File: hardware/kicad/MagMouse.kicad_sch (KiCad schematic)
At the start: 0 parts

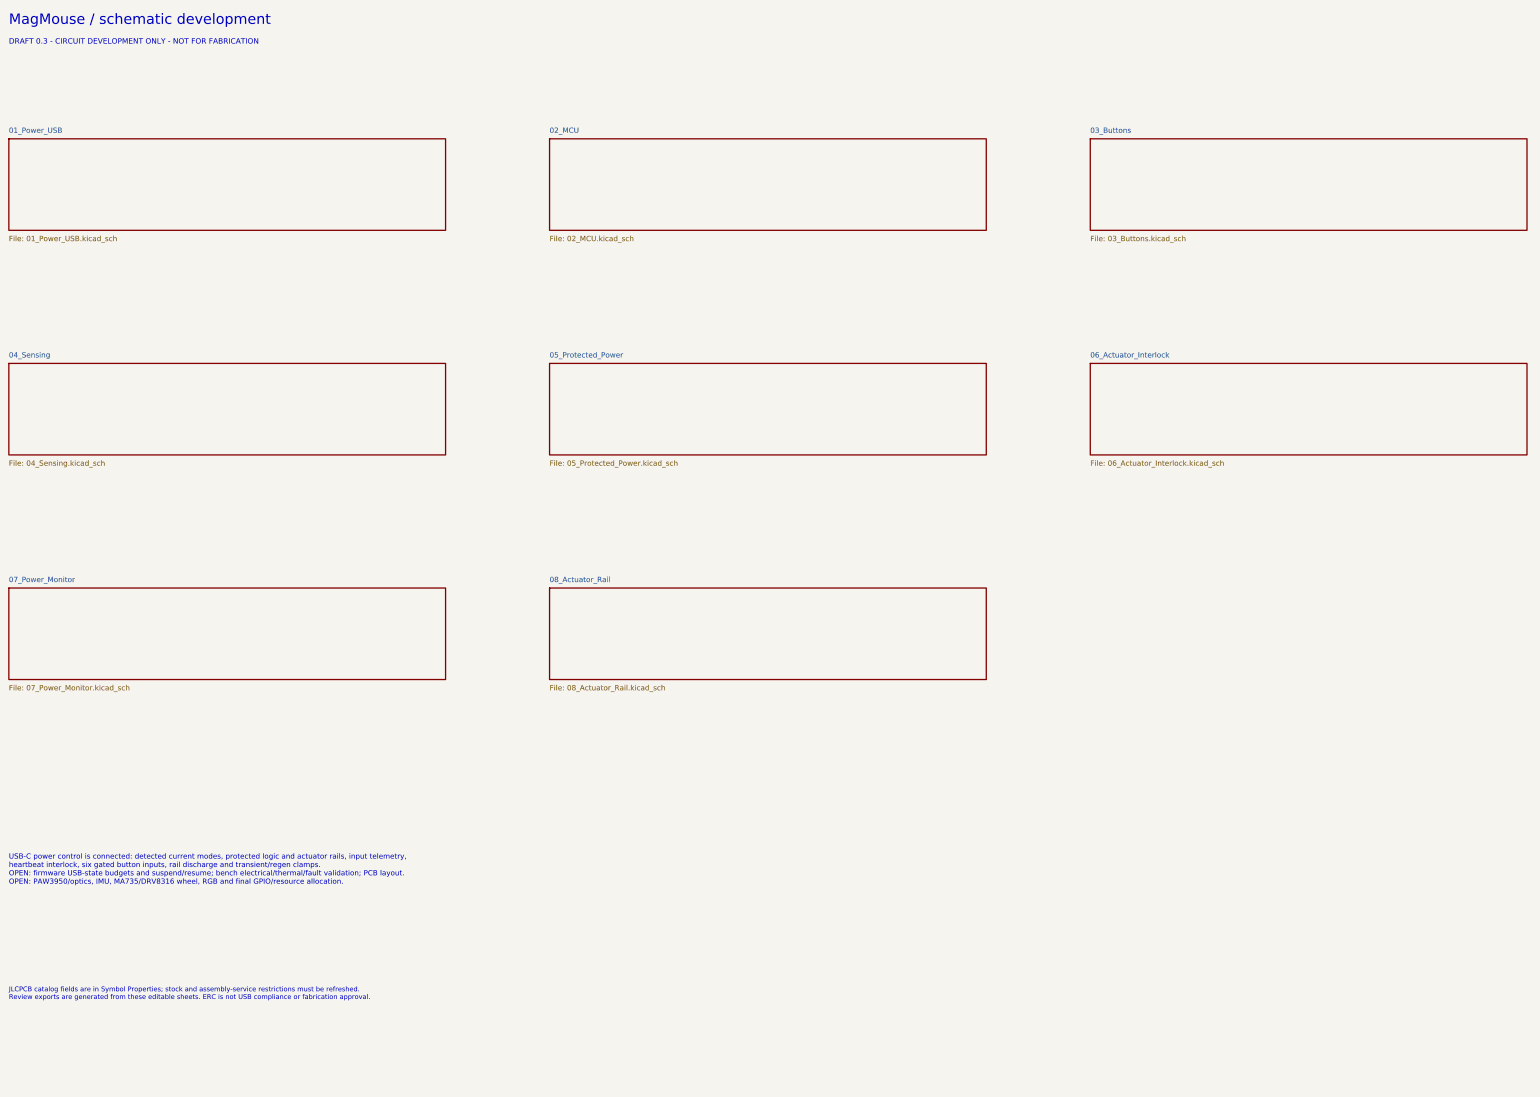
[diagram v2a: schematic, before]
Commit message: Allocate ESP32-S3 GPIO and peripheral resources
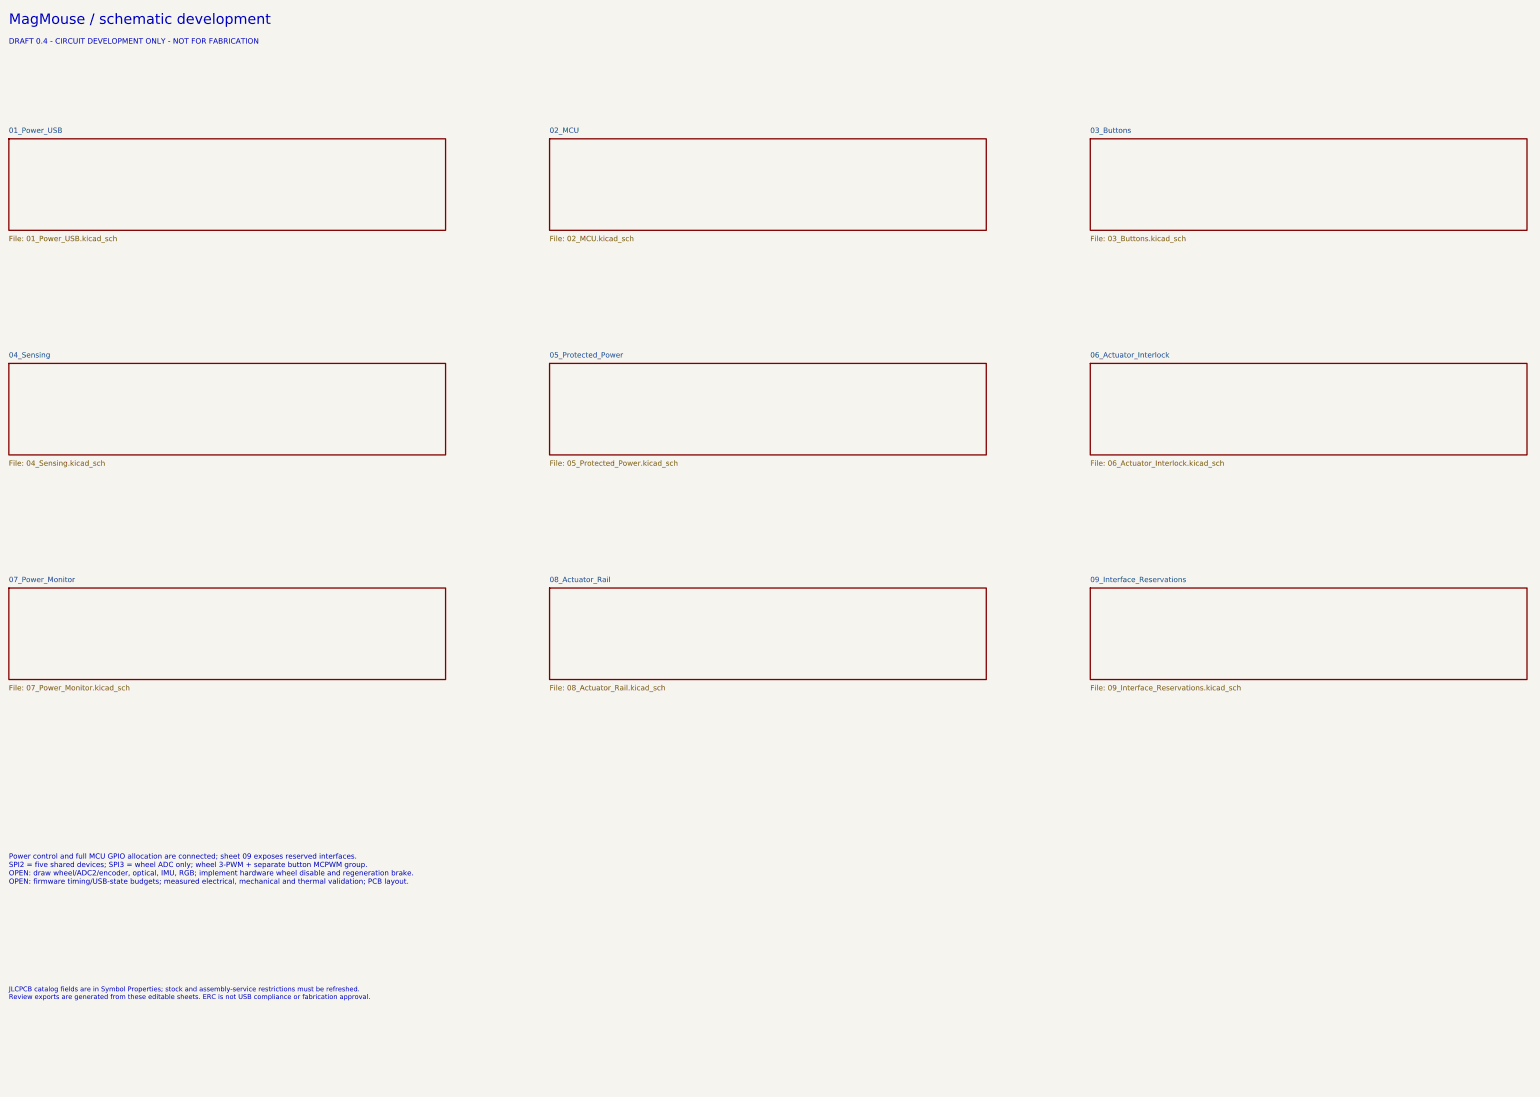
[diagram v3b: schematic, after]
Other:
- added sheet 09_Interface_Reservations (09_Interface_Reservations.kicad_sch)
- note added: "DRAFT 0.4 - CIRCUIT DEVELOPMENT ONLY - NOT FOR FABRICATION"
- note added: "Power control and full MCU GPIO allocation are connected; sheet 09 exposes reserved interfaces. SPI2 = five shared devices; SPI3 = wheel ADC only; wheel 3-PWM + separate button MCPWM group. OPEN: draw wheel/ADC2/encoder, optical, IMU, RGB; implement hardware wheel disable and regeneration brake. OPEN: firmware timing/USB-state budgets; measured electrical, mechanical and thermal validation; PCB l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"
- note removed: "DRAFT 0.3 - CIRCUIT DEVELOPMENT ONLY - NOT FOR FABRICATION"
- note removed: "USB-C power control is connected: detected current modes, protected logic and actuator rails, input telemetry, heartbeat interlock, six gated button inputs, rail discharge and transient/regen clamps. OPEN: firmware USB-state budgets and suspend/resume; bench electrical/thermal/fault validation; PCB layout. OPEN: PAW3950/optics, IMU, MA735/DRV8316 wheel, RGB and final GPIO/resource allocation."
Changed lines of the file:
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@@
     (title "MagMouse - MagMouse")
     (date "2026-09-08")
-    (rev "0.3 DRAFT")
+    (rev "0.4 DRAFT")
     (company "MagMouse")
     (comment 1 "NOT FOR FABRICATION - unresolved circuits listed in README.md"))
@@
       (justify left top))
 )
-  (text "DRAFT 0.3 - CIRCUIT DEVELOPMENT ONLY - NOT FOR FABRICATION"
+  (text "DRAFT 0.4 - CIRCUIT DEVELOPMENT ONLY - NOT FOR FABRICATION"
     (at 20 24 0)
     (effects
@@
         (path "/5d73110b-42e6-5c5c-9841-c82d60f67640"
           (page "9")))))
-  (text "USB-C power control is connected: detected current modes, protected logic and actuator rails, input telemetry,\nheartbeat interlock, six gated button inputs, rail discharge and transient/regen clamps.\nOPEN: firmware USB-state budgets and suspend/resume; bench electrical/thermal/fault validation; PCB layout.\nOPEN: PAW3950/optics, IMU, MA735/DRV8316 wheel, RGB and final GPIO/resource allocation."
+  (text "Power control and full MCU GPIO allocation are connected; sheet 09 exposes reserved interfaces.\nSPI2 = five shared devices; SPI3 = wheel ADC only; wheel 3-PWM + separate button MCPWM group.\nOPEN: draw wheel/ADC2/encoder, optical, IMU, RGB; implement hardware wheel disable and regeneration brake.\nOPEN: firmware timing/USB-state budgets; measured electrical, mechanical and thermal validation; PCB layout."
     (at 20 220 0)
     (effects
@@
     (path "/"
       (page "1")))
-  (embedded_fonts no))
+  (embedded_fonts no)
+  (sheet
+    (at 280 156)
+    (size 105 22)
+    (stroke
+      (width 0.254)
+      (type default))
+    (fill
+      (color 0 0 0 0))
+    (property "Sheetname" "09_Interface_Reservations"
+      (at 280 154.73 0)
+      (effects
+        (font
+          (size 1.27 1.27))
+        (justify left bottom)))
+    (property "Sheetfile" "09_Interface_Reservations.kicad_sch"
+      (at 280 179.27 0)
+      (effects
+        (font
+          (size 1.27 1.27))
+        (justify left top)))
+    (instances
+      (project "MagMouse"
+        (path "/5d73110b-42e6-5c5c-9841-c82d60f67640"
+          (page "10"))))))

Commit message: Add wheel control circuitry and autonomous regeneration brake
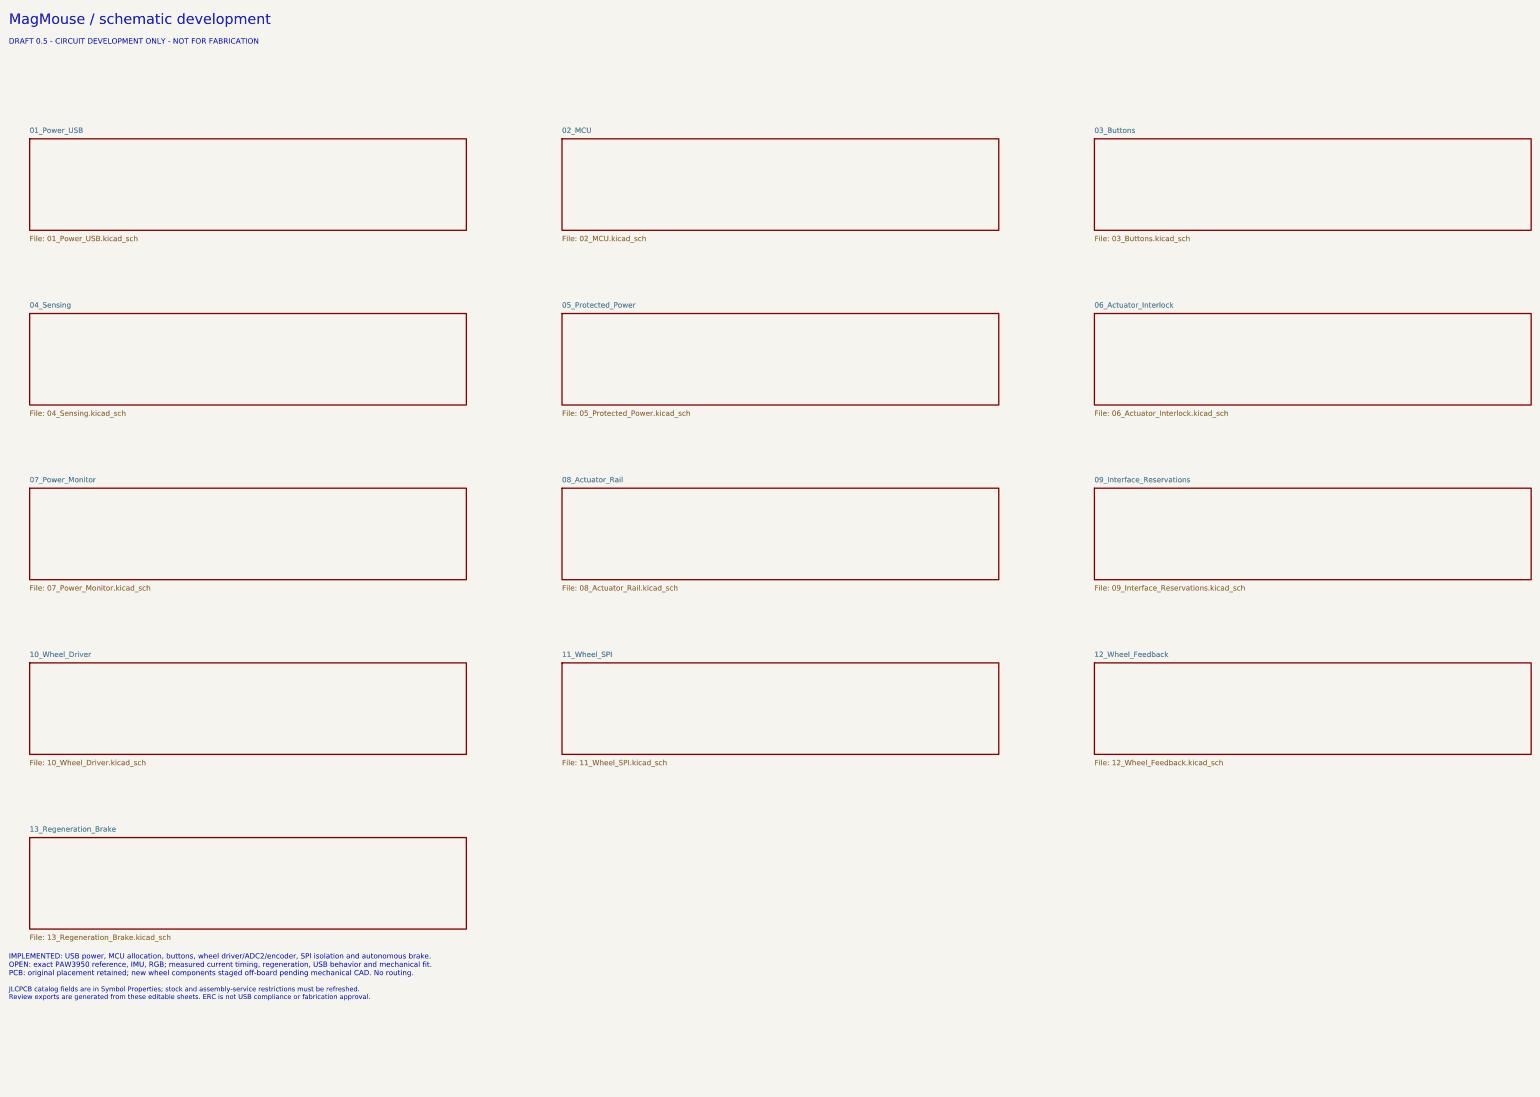
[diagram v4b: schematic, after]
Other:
- added sheet 10_Wheel_Driver (10_Wheel_Driver.kicad_sch)
- added sheet 11_Wheel_SPI (11_Wheel_SPI.kicad_sch)
- added sheet 12_Wheel_Feedback (12_Wheel_Feedback.kicad_sch)
- added sheet 13_Regeneration_Brake (13_Regeneration_Brake.kicad_sch)
- note added: "DRAFT 0.5 - CIRCUIT DEVELOPMENT ONLY - NOT FOR FABRICATION"
- note added: "IMPLEMENTED: USB power, MCU allocation, buttons, wheel driver/ADC2/encoder, SPI isolation and autonomous brake. OPEN: exact PAW3950 reference, IMU, RGB; measured current timing, regeneration, USB behavior and mechanical fit. PCB: original placement retained; new wheel components staged off-board pending mechanical CAD. No routing."
- note removed: "DRAFT 0.4 - CIRCUIT DEVELOPMENT ONLY - NOT FOR FABRICATION"
- note removed: "Power control and full MCU GPIO allocation are connected; sheet 09 exposes reserved interfaces. SPI2 = five shared devices; SPI3 = wheel ADC only; wheel 3-PWM + separate button MCPWM group. OPEN: draw wheel/ADC2/encoder, optical, IMU, RGB; implement hardware wheel disable and regeneration brake. OPEN: firmware timing/USB-state budgets; measured electrical, mechanical and thermal validation; PCB l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"
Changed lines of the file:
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@@
   (title_block
     (title "MagMouse - MagMouse")
-    (date "2026-09-08")
-    (rev "0.4 DRAFT")
+    (date "2026-09-09")
+    (rev "0.5 DRAFT")
     (company "MagMouse")
     (comment 1 "NOT FOR FABRICATION - unresolved circuits listed in README.md"))
@@
       (justify left top))
 )
-  (text "DRAFT 0.4 - CIRCUIT DEVELOPMENT ONLY - NOT FOR FABRICATION"
+  (text "DRAFT 0.5 - CIRCUIT DEVELOPMENT ONLY - NOT FOR FABRICATION"
     (at 20 24 0)
     (effects
@@
 )
   (sheet
-    (at 20 48)
+    (at 25 48)
     (size 105 22)
     (stroke
@@
       (color 0 0 0 0))
     (property "Sheetname" "01_Power_USB"
-      (at 20 46.73 0)
+      (at 25 46.73 0)
       (effects
         (font
@@
         (justify left bottom)))
     (property "Sheetfile" "01_Power_USB.kicad_sch"
-      (at 20 71.27 0)
+      (at 25 71.27 0)
       (effects
         (font
@@
           (page "2")))))
   (sheet
-    (at 150 48)
+    (at 153 48)
     (size 105 22)
     (stroke
@@
       (color 0 0 0 0))
     (property "Sheetname" "02_MCU"
-      (at 150 46.73 0)
+      (at 153 46.73 0)
       (effects
         (font
@@
         (justify left bottom)))
     (property "Sheetfile" "02_MCU.kicad_sch"
-      (at 150 71.27 0)
+      (at 153 71.27 0)
       (effects
         (font
@@
           (page "3")))))
   (sheet
-    (at 280 48)
+    (at 281 48)
     (size 105 22)
     (stroke
@@
       (color 0 0 0 0))
     (property "Sheetname" "03_Buttons"
-      (at 280 46.73 0)
+      (at 281 46.73 0)
       (effects
         (font
@@
         (justify left bottom)))
     (property "Sheetfile" "03_Buttons.kicad_sch"
-      (at 280 71.27 0)
+      (at 281 71.27 0)
       (effects
         (font
@@
           (page "4")))))
   (sheet
-    (at 20 102)
+    (at 25 90)
     (size 105 22)
     (stroke
@@
       (color 0 0 0 0))
     (property "Sheetname" "04_Sensing"
-      (at 20 100.73 0)
+      (at 25 88.73 0)
       (effects
         (font
@@
         (justify left bottom)))
     (property "Sheetfile" "04_Sensing.kicad_sch"
-      (at 20 125.27 0)
+      (at 25 113.27 0)
       (effects
         (font
@@
           (page "5")))))
   (sheet
-    (at 150 102)
+    (at 153 90)
     (size 105 22)
     (stroke
@@
       (color 0 0 0 0))
     (property "Sheetname" "05_Protected_Power"
-      (at 150 100.73 0)
+      (at 153 88.73 0)
       (effects
         (font
@@
         (justify left bottom)))
     (property "Sheetfile" "05_Protected_Power.kicad_sch"
-      (at 150 125.27 0)
+      (at 153 113.27 0)
       (effects
         (font
@@
           (page "6")))))
   (sheet
-    (at 280 102)
+    (at 281 90)
     (size 105 22)
     (stroke
@@
       (color 0 0 0 0))
     (property "Sheetname" "06_Actuator_Interlock"
-      (at 280 100.73 0)
+      (at 281 88.73 0)
       (effects
         (font
@@
         (justify left bottom)))
     (property "Sheetfile" "06_Actuator_Interlock.kicad_sch"
-      (at 280 125.27 0)
+      (at 281 113.27 0)
       (effects
         (font
@@
           (page "7")))))
   (sheet
-    (at 20 156)
+    (at 25 132)
     (size 105 22)
     (stroke
@@
       (color 0 0 0 0))
     (property "Sheetname" "07_Power_Monitor"
-      (at 20 154.73 0)
+      (at 25 130.73 0)
       (effects
         (font
@@
         (justify left bottom)))
     (property "Sheetfile" "07_Power_Monitor.kicad_sch"
-      (at 20 179.27 0)
+      (at 25 155.27 0)
       (effects
         (font
@@
           (page "8")))))
   (sheet
-    (at 150 156)
+    (at 153 132)
     (size 105 22)
     (stroke
@@
       (color 0 0 0 0))
     (property "Sheetname" "08_Actuator_Rail"
-      (at 150 154.73 0)
+      (at 153 130.73 0)
       (effects
         (font
@@
         (justify left bottom)))
     (property "Sheetfile" "08_Actuator_Rail.kicad_sch"
-      (at 150 179.27 0)
+      (at 153 155.27 0)
       (effects
         (font
@@
         (path "/5d73110b-42e6-5c5c-9841-c82d60f67640"
           (page "9")))))
-  (text "Power control and full MCU GPIO allocation are connected; sheet 09 exposes reserved interfaces.\nSPI2 = five shared devices; SPI3 = wheel ADC only; wheel 3-PWM + separate button MCPWM group.\nOPEN: draw wheel/ADC2/encoder, optical, IMU, RGB; implement hardware wheel disable and regeneration brake.\nOPEN: firmware timing/USB-state budgets; measured electrical, mechanical and thermal validation; PCB layout."
-    (at 20 220 0)
+  (text "IMPLEMENTED: USB power, MCU allocation, buttons, wheel driver/ADC2/encoder, SPI isolation and autonomous brake.\nOPEN: exact PAW3950 reference, IMU, RGB; measured current timing, regeneration, USB behavior and mechanical fit.\nPCB: original placement retained; new wheel components staged off-board pending mechanical CAD. No routing."
+    (at 20 244 0)
     (effects
       (font
@@
   (embedded_fonts no)
   (sheet
-    (at 280 156)
+    (at 281 132)
     (size 105 22)
     (stroke
@@
       (color 0 0 0 0))
     (property "Sheetname" "09_Interface_Reservations"
-      (at 280 154.73 0)
+      (at 281 130.73 0)
       (effects
         (font
@@
         (justify left bottom)))
     (property "Sheetfile" "09_Interface_Reservations.kicad_sch"
-      (at 280 179.27 0)
-      (effects
-        (font
-          (size 1.27 1.27))
-        (justify left top)))
-    (instances
-      (project "MagMouse"
-        (path "/5d73110b-42e6-5c5c-9841-c82d60f67640"
-          (page "10"))))))
+      (at 281 155.27 0)
+      (effects
+        (font
+          (size 1.27 1.27))
+        (justify left top)))
+    (instances
+      (project "MagMouse"
+        (path "/5d73110b-42e6-5c5c-9841-c82d60f67640"
+          (page "10")))))
+  (sheet
+    (at 25 174)
+    (size 105 22)
+    (stroke
+      (width 0.254)
+      (type default))
+    (fill
+      (color 0 0 0 0))
+    (property "Sheetname" "10_Wheel_Driver"
+      (at 25 172.73 0)
+      (effects
+        (font
+          (size 1.27 1.27))
+        (justify left bottom)))
+    (property "Sheetfile" "10_Wheel_Driver.kicad_sch"
+      (at 25 197.27 0)
+      (effects
+        (font
+          (size 1.27 1.27))
+        (justify left top)))
+    (instances
+      (project "MagMouse"
+        (path "/5d73110b-42e6-5c5c-9841-c82d60f67640"
+          (page "11")))))
+  (sheet
+    (at 153 174)
+    (size 105 22)
+    (stroke
+      (width 0.254)
+      (type default))
+    (fill
+      (color 0 0 0 0))
+    (property "Sheetname" "11_Wheel_SPI"
+      (at 153 172.73 0)
+      (effects
+        (font
+          (size 1.27 1.27))
+        (justify left bottom)))
+    (property "Sheetfile" "11_Wheel_SPI.kicad_sch"
+      (at 153 197.27 0)
+      (effects
+        (font
+          (size 1.27 1.27))
+        (justify left top)))
+    (instances
+      (project "MagMouse"
+        (path "/5d73110b-42e6-5c5c-9841-c82d60f67640"
+          (page "12")))))
+  (sheet
+    (at 281 174)
+    (size 105 22)
+    (stroke
+      (width 0.254)
+      (type default))
+    (fill
+      (color 0 0 0 0))
+    (property "Sheetname" "12_Wheel_Feedback"
+      (at 281 172.73 0)
+      (effects
+        (font
+          (size 1.27 1.27))
+        (justify left bottom)))
+    (property "Sheetfile" "12_Wheel_Feedback.kicad_sch"
+      (at 281 197.27 0)
+      (effects
+        (font
+          (size 1.27 1.27))
+        (justify left top)))
+    (instances
+      (project "MagMouse"
+        (path "/5d73110b-42e6-5c5c-9841-c82d60f67640"
+          (page "13")))))
+  (sheet
+    (at 25 216)
+    (size 105 22)
+    (stroke
+      (width 0.254)
+      (type default))
+    (fill
+      (color 0 0 0 0))
+    (property "Sheetname" "13_Regeneration_Brake"
+      (at 25 214.73 0)
+      (effects
+        (font
+          (size 1.27 1.27))
+        (justify left bottom)))
+    (property "Sheetfile" "13_Regeneration_Brake.kicad_sch"
+      (at 25 239.27 0)
+      (effects
+        (font
+          (size 1.27 1.27))
+        (justify left top)))
+    (instances
+      (project "MagMouse"
+        (path "/5d73110b-42e6-5c5c-9841-c82d60f67640"
+          (page "14"))))))
